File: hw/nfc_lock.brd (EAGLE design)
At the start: 48.6 x 75.6 mm, 30 parts, among them IC1 STM8S003F3, IC3 MCP170312MB, Q1 8MHz, Q3 2N7002,215, U1 M24SR16-YMN6T/2, U2 IRFML8244TRPBF, U3 IRFML8244TRPBF, X1 MINI-USB-32005-301

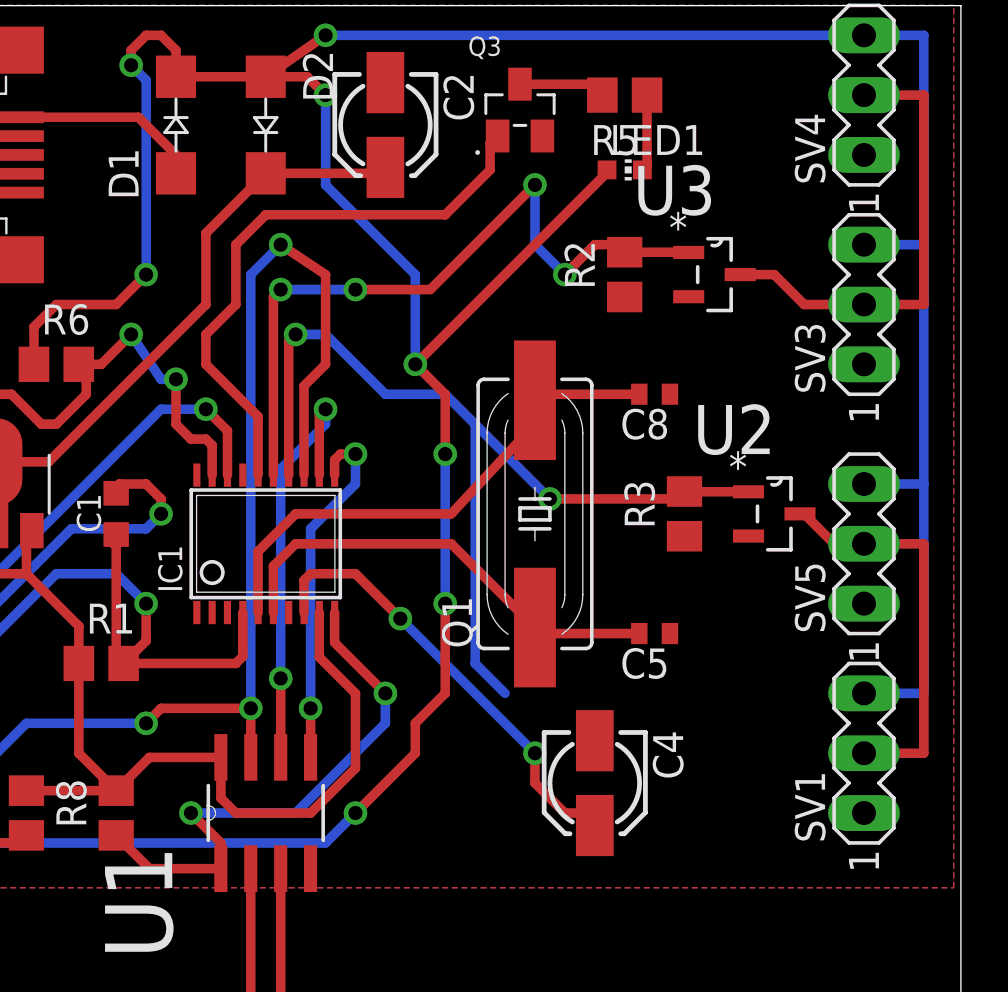
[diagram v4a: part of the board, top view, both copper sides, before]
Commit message: added on/off transistor for servos. replaced transistor for PWM servo control. added names to the most important signal lines.
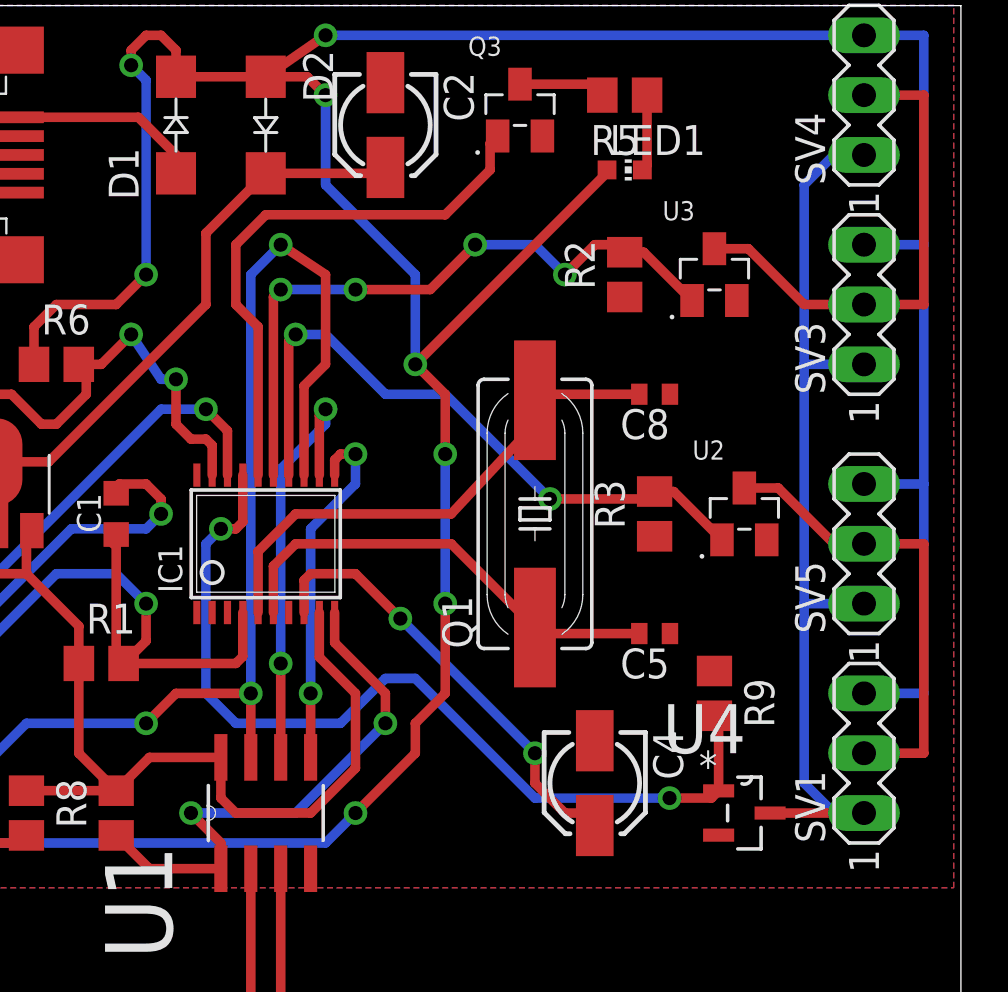
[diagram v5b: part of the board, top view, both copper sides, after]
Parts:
- added R9: 10k, rcl:R0805
- added U4: IRFML8244TRPBF, irfml8244trpbf:SOT95P240X112-3N
- U2, U3: value IRFML8244TRPBF -> 2N7002,215; device irfml8244trpbf:SOT95P240X112-3N -> Common-Parts-Library-Eagle:SOT95P230X110-3N
- moved R3 1.27 mm to (40.6, 58.4)
- moved U2 1.27 mm to (44.5, 58.4)
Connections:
- net N$1 renamed SCL
- net N$13 renamed SERVO_PACK_2
- net N$19 renamed CTRL_LED
- net N$2 renamed SDA
- net N$3 renamed SERVO_PACK_1
- new net SERVO_GND: SV1.1, SV3.1, SV4.1, SV5.1, U4.3
- new net SERWO_PWR: IC1.17, R9.2, U4.1
- net 0V: now also R9.1, U4.2; no longer SV1.1, SV3.1, SV4.1, SV5.1
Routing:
- net SERVO_GND: track 0.00 -> 40.6 mm
- net SERWO_PWR: track 0.00 -> 38.9 mm, vias 0 -> 2
- net SERVO_PACK_1: track 40.3 -> 28.1 mm
- net N$9: track 17.2 -> 20.0 mm
- net SERVO_PACK_2: track 30.9 -> 28.3 mm
- net N$11: track 19.8 -> 21.3 mm
- net CTRL_LED: track 24.9 -> 23.9 mm

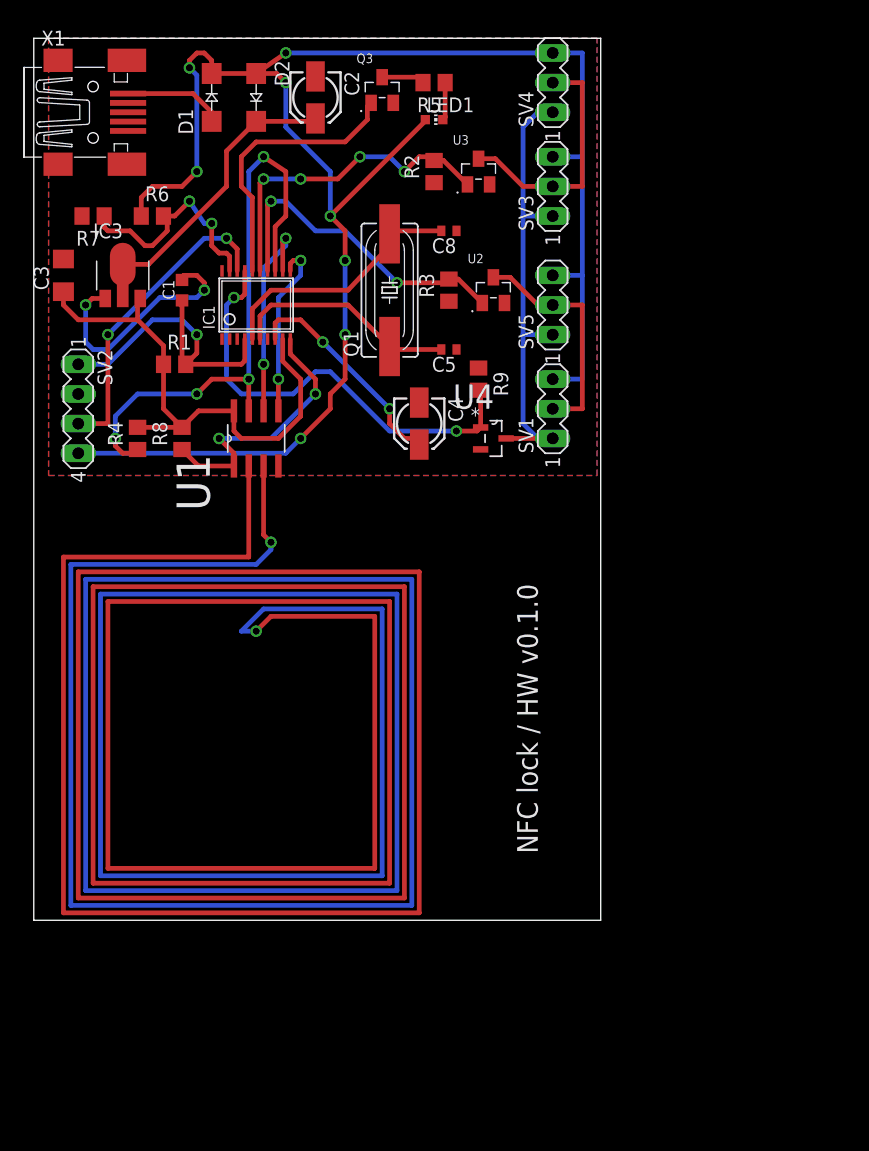
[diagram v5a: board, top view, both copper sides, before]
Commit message: added pull-ups for I2C and m24sr Vcc decoupling; changed antena type to single-sided
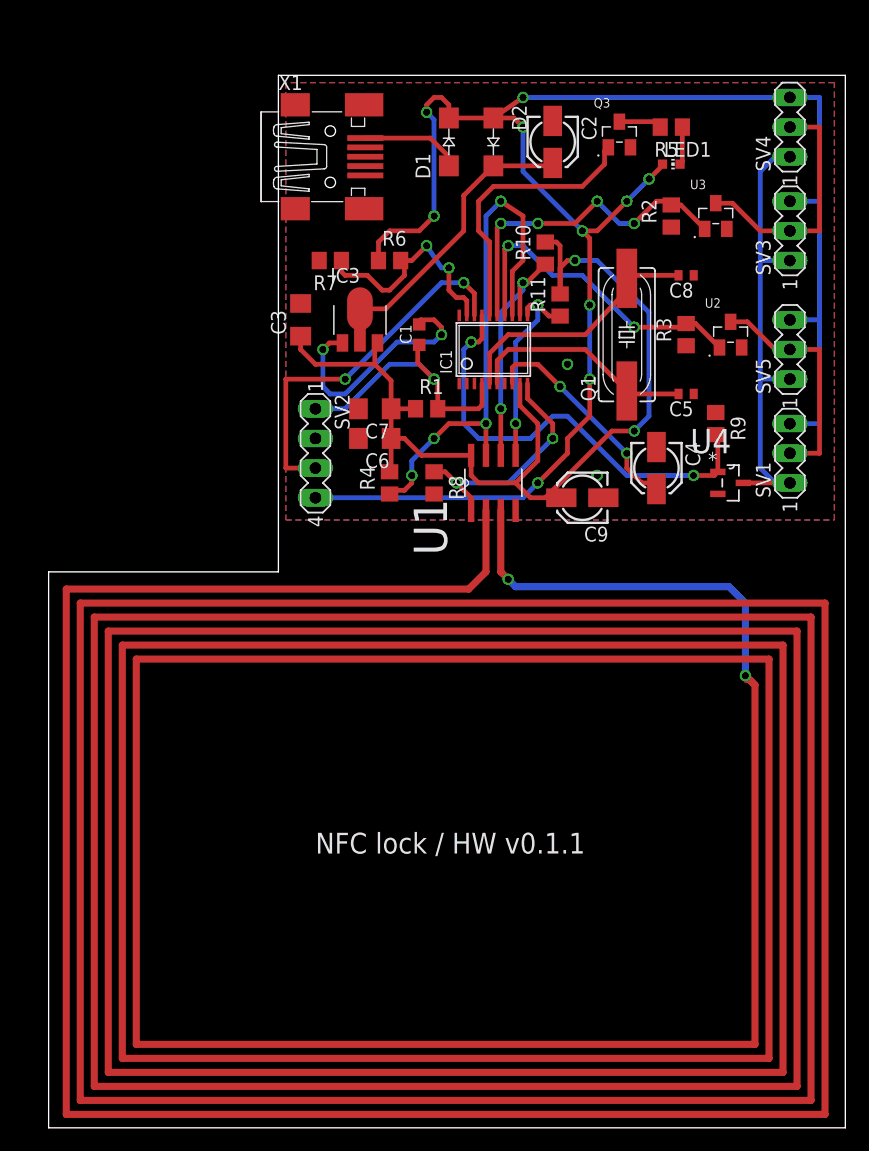
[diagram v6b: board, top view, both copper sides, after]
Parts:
- added C6: 100pF, rcl:C1206
- added C7: 100nF, rcl:C1206
- added C9: 1uF, rcl:153CLV-0405
- added R10, R11: 4.7k, rcl:R0805
- moved R4 21.9 mm to (35.6, 41.9)
- moved R1 21.9 mm to (38.7, 48.3)
- moved R8 21.9 mm to (39.4, 41.9), turned to 270 degrees
- moved D2 20.7 mm to (44.5, 71.1)
- moved IC1 20.7 mm to (44.5, 53.3)
- moved IC3 20.7 mm to (33.0, 55.9)
- moved U1 20.7 mm to (44.5, 41.9)
- moved C1 20.7 mm to (38.1, 54.6)
- moved C2 20.7 mm to (49.5, 71.1)
- moved C3 20.7 mm to (27.9, 55.9)
- moved C4 20.7 mm to (58.4, 43.2)
- moved C5 20.7 mm to (61.0, 49.5)
- moved C8 20.7 mm to (61.0, 59.7)
- moved D1 20.7 mm to (40.6, 71.1)
- moved LED1 20.7 mm to (59.7, 69.2)
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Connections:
- net +5V/1: now also C6.1, C7.1, C9.+, R10.2, R11.2; no longer R8.2
- net 0V: now also C6.2, C7.2, C9.-, R8.2
- net SCL: now also R10.1
- net SDA: now also R11.1
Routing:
- net ANTENA: track 758.1 -> 1186.2 mm
- net +5V/1: track 45.3 -> 87.7 mm, vias 0 -> 2
- net N$8: track 51.1 -> 45.3 mm
- net N$6: track 26.9 -> 32.0 mm
- net N$5: track 28.3 -> 24.2 mm
- net N$7: track 23.3 -> 20.6 mm
- net SCL: track 18.5 -> 21.0 mm
- net SDA: track 15.3 -> 17.6 mm
- net +5V/2: track 156.7 -> 154.9 mm, vias 8 -> 10
- net SERVO_PACK_2: track 28.3 -> 28.8 mm
- net 0V: vias 2 -> 4
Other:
- board size 48.6 x 75.6 mm -> 68.2 x 90.2 mm
- board text added: "NFC lock / HW v0.1.1"
- board text removed: "NFC lock / HW v0.1.0"

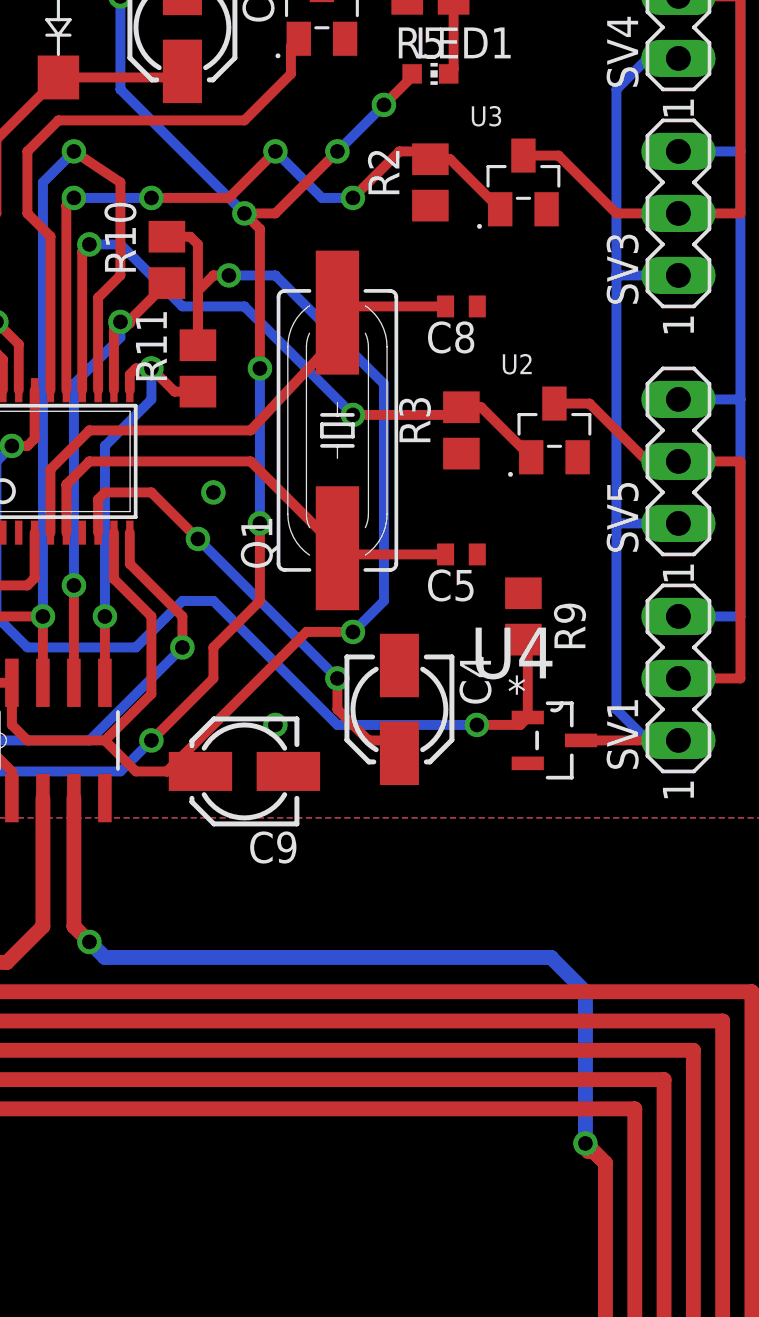
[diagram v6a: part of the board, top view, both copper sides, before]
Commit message: lcearence and spacing fixed
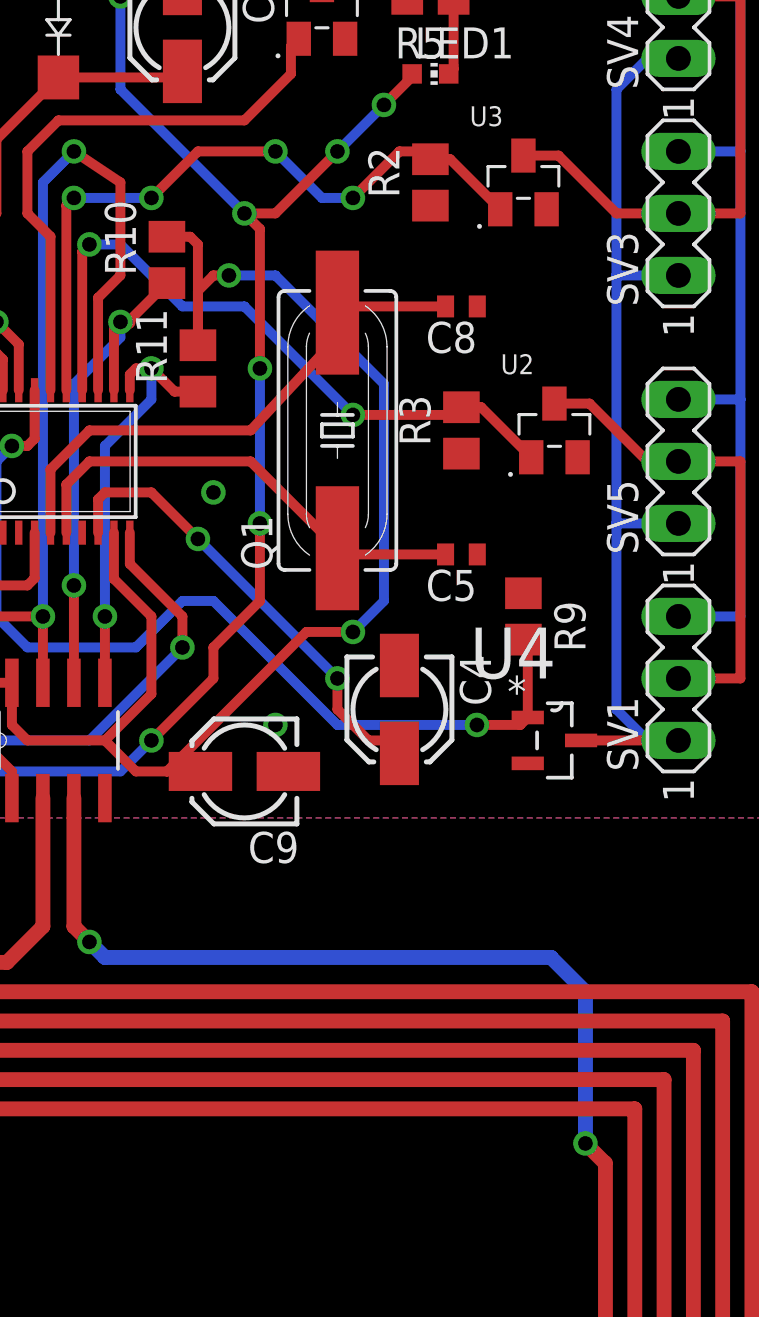
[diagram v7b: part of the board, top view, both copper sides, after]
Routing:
- net ANTENA: track 1186.2 -> 1185.4 mm
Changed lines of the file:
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@@
 <contactref element="U1" pad="2"/>
 <via x="66.04" y="25.4" extent="1-16" drill="0.6"/>
-<wire x1="66.04" y1="25.4" x2="66.675" y2="24.765" width="0.6096" layer="1"/>
-<wire x1="66.86041875" y1="24.5999" x2="66.144140625" y2="25.313640625" width="0.6096" layer="1"/>
 <wire x1="66.86041875" y1="-6.1849" x2="66.86041875" y2="24.5999" width="0.6096" layer="1"/>
 <wire x1="66.86041875" y1="-6.1849" x2="13.86078125" y2="-6.1849" width="0.6096" layer="1"/>
@@
 <wire x1="64.63538125" y1="33.02" x2="66.04" y2="31.61538125" width="0.6096" layer="16"/>
 <wire x1="66.04" y1="31.61538125" x2="66.04" y2="25.4" width="0.6096" layer="16"/>
+<wire x1="66.86041875" y1="24.5999" x2="66.8401" y2="24.5999" width="0.4064" layer="1"/>
+<wire x1="66.8401" y1="24.5999" x2="66.04" y2="25.4" width="0.6096" layer="1"/>
 </signal>
 <signal name="SERVO_PACK_2">
@@
 <wire x1="45.085" y1="64.135" x2="48.26" y2="64.135" width="0.4064" layer="16"/>
 <via x="48.26" y="64.135" extent="1-16" drill="0.6"/>
-<wire x1="48.26" y1="64.135" x2="51.435" y2="64.135" width="0.4064" layer="1"/>
-<wire x1="51.435" y1="64.135" x2="53.34" y2="66.04" width="0.4064" layer="1"/>
+<wire x1="48.26" y1="64.135" x2="50.165" y2="66.04" width="0.4064" layer="1"/>
+<wire x1="50.165" y1="66.04" x2="53.34" y2="66.04" width="0.4064" layer="1"/>
 <via x="53.34" y="66.04" extent="1-16" drill="0.6"/>
 <wire x1="44.775" y1="56.2578" x2="44.775" y2="63.825" width="0.4064" layer="1"/>
@@
 </signal>
 <signal name="S$1348">
-<wire x1="66.144140625" y1="25.562559375" x2="66.144140625" y2="25.06471875" width="0.6096" layer="1"/>
 </signal>
 </signals>
